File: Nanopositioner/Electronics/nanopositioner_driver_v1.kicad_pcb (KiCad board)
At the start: 2 copper layers, 9 parts, among them IC1 DLPC1438ZEZ, U1 ISO7720D, U2 DAC8552, U3 DAC8552, U4 STM32G431CBTx, U5 OPA552U, U6 ISO7720D, U7 OPA552U, U8 OPA552U

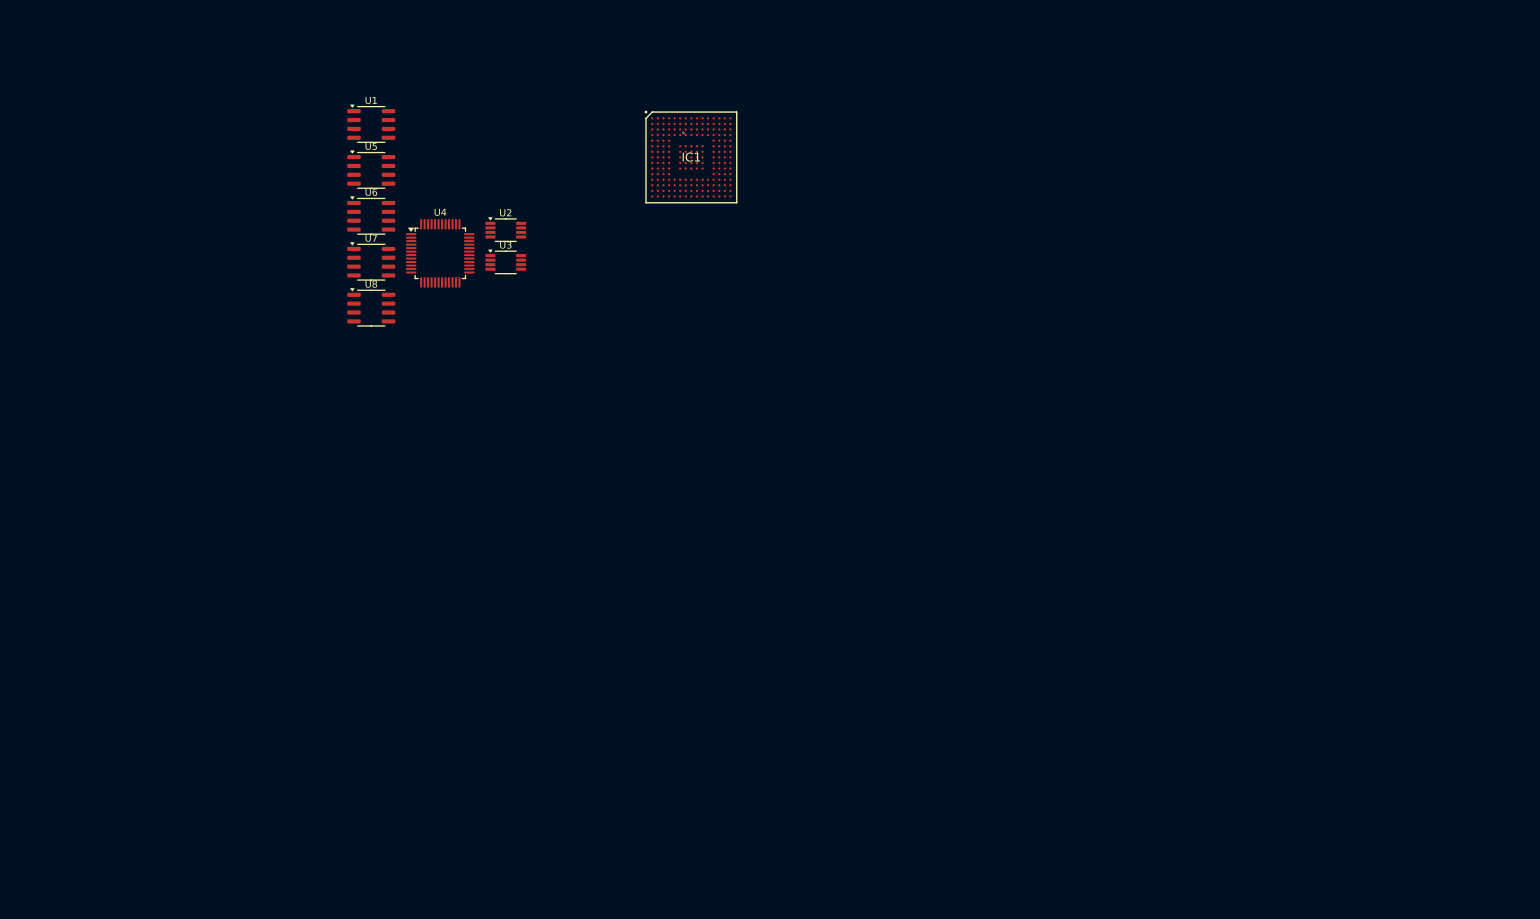
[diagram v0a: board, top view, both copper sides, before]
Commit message: Updated driver design
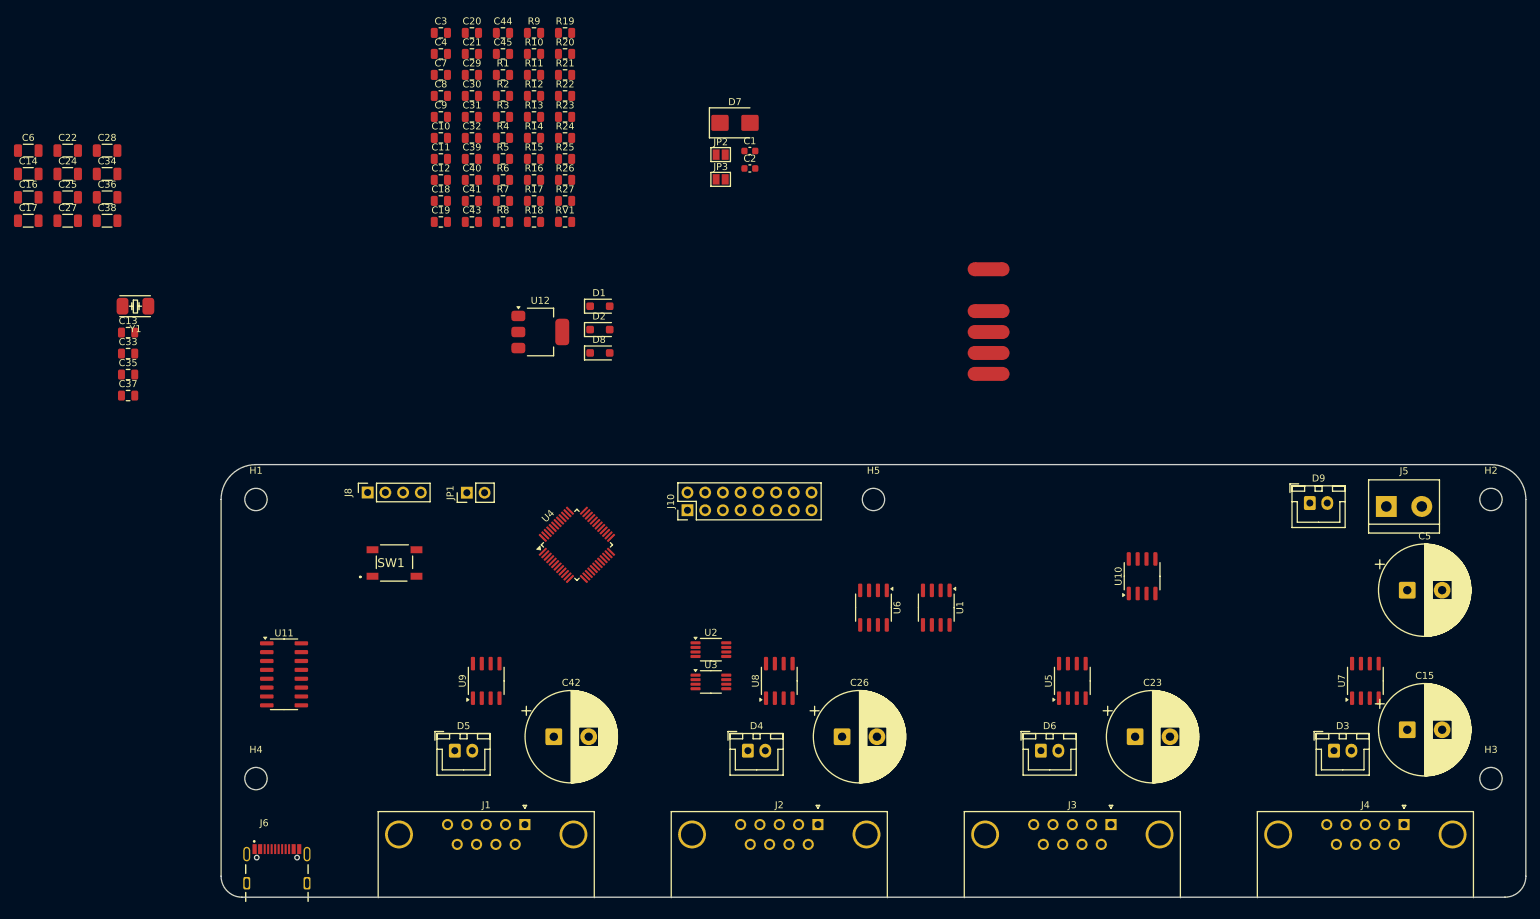
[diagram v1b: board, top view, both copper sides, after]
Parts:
- removed IC1: DLPC1438ZEZ, SamacSys_Parts:BGA201C80P15X15_1300X1300X100
- added C1: 22p, Capacitor_SMD:C_0603_1608Metric, F.Cu at (143.8, 38.0)
- added C10: 100n, Capacitor_SMD:C_0805_2012Metric, F.Cu at (99.5, 36.2)
- added C11: 100n, Capacitor_SMD:C_0805_2012Metric, F.Cu at (99.5, 39.2)
- added C12: 100n, Capacitor_SMD:C_0805_2012Metric, F.Cu at (99.5, 42.2)
- added C13: 100n 100V, Capacitor_SMD:C_0805_2012Metric, F.Cu at (54.7, 64.1)
- added C14: 1u 100V, Capacitor_SMD:C_1206_3216Metric, F.Cu at (40.4, 41.4)
- added C15: 220u 100V, Capacitor_THT:CP_Radial_D13.0mm_P5.00mm, F.Cu at (238.0, 121.0)
- added C16: 1u 100V, Capacitor_SMD:C_1206_3216Metric, F.Cu at (40.4, 44.7)
- added C17: 1u 100V, Capacitor_SMD:C_1206_3216Metric, F.Cu at (40.4, 48.0)
- added C18: 10u, Capacitor_SMD:C_0805_2012Metric, F.Cu at (99.5, 45.2)
- added C19: 10u, Capacitor_SMD:C_0805_2012Metric, F.Cu at (99.5, 48.2)
- added C2: 22p, Capacitor_SMD:C_0603_1608Metric, F.Cu at (143.8, 40.6)
- added C20: 10u, Capacitor_SMD:C_0805_2012Metric, F.Cu at (104.0, 21.1)
- added C21: 10u, Capacitor_SMD:C_0805_2012Metric, F.Cu at (104.0, 24.1)
- added C22: 1u 100V, Capacitor_SMD:C_1206_3216Metric, F.Cu at (46.0, 38.0)
- added C23: 220u 100V, Capacitor_THT:CP_Radial_D13.0mm_P5.00mm, F.Cu at (199.0, 122.0)
- added C24: 1u 100V, Capacitor_SMD:C_1206_3216Metric, F.Cu at (46.0, 41.4)
- added C25: 1u 100V, Capacitor_SMD:C_1206_3216Metric, F.Cu at (46.0, 44.7)
- added C26: 220u 100V, Capacitor_THT:CP_Radial_D13.0mm_P5.00mm, F.Cu at (157.0, 122.0)
- added C27: 1u 100V, Capacitor_SMD:C_1206_3216Metric, F.Cu at (46.0, 48.0)
- added C28: 1u 100V, Capacitor_SMD:C_1206_3216Metric, F.Cu at (51.7, 38.0)
- added C29: 10u, Capacitor_SMD:C_0805_2012Metric, F.Cu at (104.0, 27.1)
- added C3: 100n, Capacitor_SMD:C_0805_2012Metric, F.Cu at (99.5, 21.1)
- added C30: 100n, Capacitor_SMD:C_0805_2012Metric, F.Cu at (104.0, 30.2)
- added C31: 10u, Capacitor_SMD:C_0805_2012Metric, F.Cu at (104.0, 33.2)
- added C32: 100n, Capacitor_SMD:C_0805_2012Metric, F.Cu at (104.0, 36.2)
- added C33: 100n 100V, Capacitor_SMD:C_0805_2012Metric, F.Cu at (54.7, 67.1)
- added C34: 1u 100V, Capacitor_SMD:C_1206_3216Metric, F.Cu at (51.7, 41.4)
- added C35: 100n 100V, Capacitor_SMD:C_0805_2012Metric, F.Cu at (54.7, 70.1)
- added C36: 1u 100V, Capacitor_SMD:C_1206_3216Metric, F.Cu at (51.7, 44.7)
- added C37: 100n 100V, Capacitor_SMD:C_0805_2012Metric, F.Cu at (54.7, 73.1)
- added C38: 1u 100V, Capacitor_SMD:C_1206_3216Metric, F.Cu at (51.7, 48.0)
- added C39: 10u, Capacitor_SMD:C_0805_2012Metric, F.Cu at (104.0, 39.2)
- added C4: 10u, Capacitor_SMD:C_0805_2012Metric, F.Cu at (99.5, 24.1)
- added C40: 100n, Capacitor_SMD:C_0805_2012Metric, F.Cu at (104.0, 42.2)
- added C41: 100n, Capacitor_SMD:C_0805_2012Metric, F.Cu at (104.0, 45.2)
- added C42: 220u 100V, Capacitor_THT:CP_Radial_D13.0mm_P5.00mm, F.Cu at (115.7, 122.0)
- added C43: 100n, Capacitor_SMD:C_0805_2012Metric, F.Cu at (104.0, 48.2)
- added C44: 10u, Capacitor_SMD:C_0805_2012Metric, F.Cu at (108.4, 21.1)
- added C45: 10u, Capacitor_SMD:C_0805_2012Metric, F.Cu at (108.4, 24.1)
- added C5: 220u 100V, Capacitor_THT:CP_Radial_D13.0mm_P5.00mm, F.Cu at (238.0, 101.0)
- added C6: 1u 100V, Capacitor_SMD:C_1206_3216Metric, F.Cu at (40.4, 38.0)
- added C7: 100n, Capacitor_SMD:C_0805_2012Metric, F.Cu at (99.5, 27.1)
- added C8: 100n, Capacitor_SMD:C_0805_2012Metric, F.Cu at (99.5, 30.2)
- added C9: 100n, Capacitor_SMD:C_0805_2012Metric, F.Cu at (99.5, 33.2)
- added D1: BZT52-C5V6, Diode_SMD:D_SOD-123F, F.Cu at (122.3, 60.3)
- added D2: BZT52-C5V6, Diode_SMD:D_SOD-123F, F.Cu at (122.3, 63.6)
- added D3: LED_Small, Connector_JST:JST_XH_B2B-XH-A_1x02_P2.50mm_Vertical, F.Cu at (227.5, 124.0)
- added D4: LED_Small, Connector_JST:JST_XH_B2B-XH-A_1x02_P2.50mm_Vertical, F.Cu at (143.5, 124.0)
- added D5: LED_Small, Connector_JST:JST_XH_B2B-XH-A_1x02_P2.50mm_Vertical, F.Cu at (101.5, 124.0)
- added D6: LED_Small, Connector_JST:JST_XH_B2B-XH-A_1x02_P2.50mm_Vertical, F.Cu at (185.5, 124.0)
- added D7: SS310, Diode_SMD:D_SMB, F.Cu at (141.6, 34.0)
- added D8: BZT52-B75, Diode_SMD:D_SOD-123F, F.Cu at (122.3, 67.0)
- added D9: OVP_INDICATOR, Connector_JST:JST_XH_B2B-XH-A_1x02_P2.50mm_Vertical, F.Cu at (224.0, 88.5)
- added H1: MountingHole, MountingHole:MountingHole_3.2mm_M3, F.Cu at (73.0, 88.0)
- added H2: MountingHole, MountingHole:MountingHole_3.2mm_M3, F.Cu at (250.0, 88.0)
- added H3: MountingHole, MountingHole:MountingHole_3.2mm_M3, F.Cu at (250.0, 128.0)
- added H4: MountingHole, MountingHole:MountingHole_3.2mm_M3, F.Cu at (73.0, 128.0)
- added H5: MountingHole, MountingHole:MountingHole_3.2mm_M3, F.Cu at (161.5, 88.0)
- added J1: DE9_Pins, Connector_Dsub:DSUB-9_Socket_Horizontal_P2.77x2.84mm_EdgePinOffset7.70mm_Housed_MountingHolesOffset9.12mm, F.Cu at (111.5, 134.6)
- added J10: Conn_02x08_Odd_Even, Connector_PinHeader_2.54mm:PinHeader_2x08_P2.54mm_Vertical, F.Cu at (134.8, 89.5)
- added J2: DE9_Pins, Connector_Dsub:DSUB-9_Socket_Horizontal_P2.77x2.84mm_EdgePinOffset7.70mm_Housed_MountingHolesOffset9.12mm, F.Cu at (153.5, 134.6)
- added J3: DE9_Pins, Connector_Dsub:DSUB-9_Socket_Horizontal_P2.77x2.84mm_EdgePinOffset7.70mm_Housed_MountingHolesOffset9.12mm, F.Cu at (195.5, 134.6)
- added J4: DE9_Pins, Connector_Dsub:DSUB-9_Socket_Horizontal_P2.77x2.84mm_EdgePinOffset7.70mm_Housed_MountingHolesOffset9.12mm, F.Cu at (237.5, 134.6)
- added J5: HV_IN, TerminalBlock:TerminalBlock_bornier-2_P5.08mm, F.Cu at (235.0, 89.0)
- added J6: USB_UART_RECEPTACLE, SamacSys_Parts:GCT_USB4105GFA120, F.Cu at (76.0, 143.0)
- added J8: SWD, Connector_PinSocket_2.54mm:PinSocket_1x04_P2.54mm_Vertical, F.Cu at (89.0, 87.0)
- added JP1: BOOT0, Connector_PinHeader_2.54mm:PinHeader_1x02_P2.54mm_Vertical, F.Cu at (103.2, 87.0)
- added JP2: 5V_TEST, Jumper:SolderJumper-2_P1.3mm_Open_Pad1.0x1.5mm, F.Cu at (139.6, 38.6)
- added JP3: 6V2_TEST, Jumper:SolderJumper-2_P1.3mm_Open_Pad1.0x1.5mm, F.Cu at (139.6, 42.1)
- added NT2: VDDA, NetTie:NetTie-2_SMD_Pad2.0mm, F.Cu at (178.0, 55.0)
- added NT4: NetTie_2, NetTie:NetTie-2_SMD_Pad2.0mm, F.Cu at (178.0, 61.0)
- added NT5: NetTie_2, NetTie:NetTie-2_SMD_Pad2.0mm, F.Cu at (178.0, 64.0)
- added NT6: NetTie_2, NetTie:NetTie-2_SMD_Pad2.0mm, F.Cu at (178.0, 67.0)
- added NT7: NetTie_2, NetTie:NetTie-2_SMD_Pad2.0mm, F.Cu at (178.0, 70.0)
- added R1: 20k, Capacitor_SMD:C_0805_2012Metric, F.Cu at (108.4, 27.1)
- added R10: 180k, Capacitor_SMD:C_0805_2012Metric, F.Cu at (112.8, 24.1)
- added R11: 200, Capacitor_SMD:C_0805_2012Metric, F.Cu at (112.8, 27.1)
- added R12: 20k, Capacitor_SMD:C_0805_2012Metric, F.Cu at (112.8, 30.2)
- added R13: 200, Capacitor_SMD:C_0805_2012Metric, F.Cu at (112.8, 33.2)
- added R14: 200, Capacitor_SMD:C_0805_2012Metric, F.Cu at (112.8, 36.2)
- added R15: 200, Capacitor_SMD:C_0805_2012Metric, F.Cu at (112.8, 39.2)
- added R16: 180k, Capacitor_SMD:C_0805_2012Metric, F.Cu at (112.8, 42.2)
- added R17: 20k, Capacitor_SMD:C_0805_2012Metric, F.Cu at (112.8, 45.2)
- added R18: 20k, Capacitor_SMD:C_0805_2012Metric, F.Cu at (112.8, 48.2)
- added R19: 1k, Capacitor_SMD:C_0805_2012Metric, F.Cu at (117.3, 21.1)
- added R2: 180k, Capacitor_SMD:C_0805_2012Metric, F.Cu at (108.4, 30.2)
- added R20: 1k, Capacitor_SMD:C_0805_2012Metric, F.Cu at (117.3, 24.1)
- added R21: 1k, Capacitor_SMD:C_0805_2012Metric, F.Cu at (117.3, 27.1)
- added R22: 1k, Capacitor_SMD:C_0805_2012Metric, F.Cu at (117.3, 30.2)
- added R23: 10M, Capacitor_SMD:C_0805_2012Metric, F.Cu at (117.3, 33.2)
- added R24: 100k, Capacitor_SMD:C_0805_2012Metric, F.Cu at (117.3, 36.2)
- added R25: 5k49, Capacitor_SMD:C_0805_2012Metric, F.Cu at (117.3, 39.2)
- added R26: 5k49, Capacitor_SMD:C_0805_2012Metric, F.Cu at (117.3, 42.2)
- added R27: 100k, Capacitor_SMD:C_0805_2012Metric, F.Cu at (117.3, 45.2)
- added R3: 10k, Capacitor_SMD:C_0805_2012Metric, F.Cu at (108.4, 33.2)
- added R4: 0, Capacitor_SMD:C_0805_2012Metric, F.Cu at (108.4, 36.2)
- added R5: 0, Capacitor_SMD:C_0805_2012Metric, F.Cu at (108.4, 39.2)
- added R6: 180k, Capacitor_SMD:C_0805_2012Metric, F.Cu at (108.4, 42.2)
- added R7: 20k, Capacitor_SMD:C_0805_2012Metric, F.Cu at (108.4, 45.2)
- added R8: 10k, Capacitor_SMD:C_0805_2012Metric, F.Cu at (108.4, 48.2)
- added R9: 20k, Capacitor_SMD:C_0805_2012Metric, F.Cu at (112.8, 21.1)
- added RV1: 1M, Capacitor_SMD:C_0805_2012Metric, F.Cu at (117.3, 48.2)
- added SW1: NRST, SamacSys_Parts:TL3342F260QG, F.Cu at (92.8, 97.1)
- added U10: REF5050AD, Package_SO:SOIC-8_3.9x4.9mm_P1.27mm, F.Cu at (200.0, 99.0)
- added U11: CH340C, Package_SO:SOIC-16_3.9x9.9mm_P1.27mm, F.Cu at (77.0, 113.1)
- added U12: AMS1117-3.3, Package_TO_SOT_SMD:SOT-223-3_TabPin2, F.Cu at (113.8, 64.0)
- added U9: OPA552U, Package_SO:SOIC-8_3.9x4.9mm_P1.27mm, F.Cu at (106.0, 114.0)
- added Y1: 8MHz, SamacSys_Parts:YSX530, F.Cu at (55.7, 60.3)
- moved U7 154.6 mm to (232.0, 114.0), turned to 90 degrees
- moved U5 124.3 mm to (190.0, 114.0), turned to 90 degrees
- moved U1 106.5 mm to (170.5, 103.5), turned to -90 degrees
- moved U6 91.3 mm to (161.5, 103.5), turned to -90 degrees
- moved U8 79.2 mm to (148.0, 114.0), turned to 90 degrees
- moved U2 66.9 mm to (138.2, 109.5)
- moved U3 66.9 mm to (138.2, 114.2)
- moved U4 46.1 mm to (119.0, 94.5), turned to 45 degrees
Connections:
- net Net-(U1-OUTA) renamed /~{SYNC1}
- net Net-(U1-OUTB) renamed /~{SYNC2}
- net Net-(U2-D_{IN}) renamed /DIN
- net Net-(U2-SCLK) renamed /SCLK
- U1 pad 1: unconnected-(U1-VCC1-Pad1) -> +3V3
- U2 pad 1: unconnected-(U2-V_{DD}-Pad1) -> +5V_HV
- U2 pad 2: unconnected-(U2-V_{REF}-Pad2) -> +5V_REF
- U3 pad 1: unconnected-(U3-V_{DD}-Pad1) -> +5V_HV
- U3 pad 2: unconnected-(U3-V_{REF}-Pad2) -> +5V_REF
- U3 pad 3: unconnected-(U3-V_{OUT}B-Pad3) -> /PIEZO_CH4_SIG
- U4 pad 1: /VDD -> +3V3
- U4 pad 10: unconnected-(U4-PA2-Pad10) -> /UART2_TX
- U4 pad 11: unconnected-(U4-PA3-Pad11) -> /UART2_RX
- U4 pad 16: unconnected-(U4-PB0-Pad16) -> /PB0
- U4 pad 17: unconnected-(U4-PB1-Pad17) -> /~{CS4}
- U4 pad 18: unconnected-(U4-PB2-Pad18) -> /~{CS3}
- U4 pad 2: unconnected-(U4-PC13-Pad2) -> /PC13
- U4 pad 21: /VDDA -> +3V3
- U4 pad 22: unconnected-(U4-PB10-Pad22) -> /BTN3
- U4 pad 24: /VDD -> +3V3
- U4 pad 25: unconnected-(U4-PB11-Pad25) -> /~{CS2}
- U4 pad 26: unconnected-(U4-PB12-Pad26) -> /~{CS1}
- U4 pad 27: unconnected-(U4-PB13-Pad27) -> /CLK1_2
- U4 pad 28: unconnected-(U4-PB14-Pad28) -> /DO1
- U4 pad 29: unconnected-(U4-PB15-Pad29) -> /DIN1
- U4 pad 3: unconnected-(U4-PC14-Pad3) -> /PC14
- U4 pad 30: unconnected-(U4-PA8-Pad30) -> /CONN_TEST_1_P
- U4 pad 31: unconnected-(U4-PA9-Pad31) -> /CONN_TEST_2_P
- U4 pad 32: unconnected-(U4-PA10-Pad32) -> /CONN_TEST_3_P
- U4 pad 33: unconnected-(U4-PA11-Pad33) -> /CONN_TEST_4_P
- U4 pad 34: unconnected-(U4-PA12-Pad34) -> /BTN1
- U4 pad 36: /VDD -> +3V3
- U4 pad 37: unconnected-(U4-PA13-Pad37) -> /SWDIO
- U4 pad 38: unconnected-(U4-PA14-Pad38) -> /SWCLK
- U4 pad 39: unconnected-(U4-PA15-Pad39) -> /BTN4
- U4 pad 4: unconnected-(U4-PC15-Pad4) -> /PC15
- U4 pad 40: unconnected-(U4-PB3-Pad40) -> /CLK3_4
- U4 pad 41: unconnected-(U4-PB4-Pad41) -> /DO3
- U4 pad 42: unconnected-(U4-PB5-Pad42) -> /DIN3
- U4 pad 43: unconnected-(U4-PB6-Pad43) -> /UART1_TX
- U4 pad 44: unconnected-(U4-PB7-Pad44) -> /UART1_RX
- U4 pad 46: unconnected-(U4-PB9-Pad46) -> /BTN2
- U4 pad 48: /VDD -> +3V3
- U4 pad 8: unconnected-(U4-PA0-Pad8) -> /BTN5
- U4 pad 9: unconnected-(U4-PA1-Pad9) -> /BTN6
- U5 pad 2: unconnected-(U5---Pad2) -> Net-(U5--)
- U5 pad 6: unconnected-(U5-Pad6) -> Net-(Q3-B)
- U6 pad 1: unconnected-(U6-VCC1-Pad1) -> +3V3
- U7 pad 2: unconnected-(U7---Pad2) -> Net-(U7--)
- U7 pad 3: /PIEZO_CH2_SIG -> /PIEZO_CH4_SIG
- U7 pad 6: unconnected-(U7-Pad6) -> Net-(Q5-B)
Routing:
- net unconnected-(IC1-VDD_4-PadD7): track 0.51 -> 0.00 mm, vias 1 -> 0
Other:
- board outline added: 187 x 62 mm
- board text added: "High Voltage"
- board text added: "Low Voltage"

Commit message: Updated the complete PCB design
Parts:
- removed NT2: VDDA, NetTie:NetTie-2_SMD_Pad2.0mm
- removed NT4, NT5, NT6, NT7: NetTie_2, NetTie:NetTie-2_SMD_Pad2.0mm
- removed R17, R18: 20k, Capacitor_SMD:C_0805_2012Metric
- added C46: 100n, Capacitor_SMD:C_0805_2012Metric, F.Cu at (163.7, 99.6)
- added C47: 100n, Capacitor_SMD:C_0805_2012Metric, F.Cu at (172.7, 99.6)
- added C48: 100n, Capacitor_SMD:C_0805_2012Metric, F.Cu at (165.5, 109.2)
- added C49: 100n, Capacitor_SMD:C_0805_2012Metric, F.Cu at (174.5, 109.2)
- added C50: 220p 100V, Capacitor_SMD:C_1206_3216Metric, F.Cu at (237.6, 115.1)
- added C51: C_CAP, Capacitor_SMD:C_0805_2012Metric, F.Cu at (243.0, 115.4)
- added C52: C_CAP, Capacitor_SMD:C_0805_2012Metric, F.Cu at (200.3, 114.7)
- added C53: 220p 100V, Capacitor_SMD:C_1206_3216Metric, F.Cu at (196.1, 114.8)
- added C54: C_CAP, Capacitor_SMD:C_0805_2012Metric, F.Cu at (158.5, 114.8)
- added C55: 220p 100V, Capacitor_SMD:C_1206_3216Metric, F.Cu at (154.1, 114.8)
- added C56: C_CAP, Capacitor_SMD:C_0805_2012Metric, F.Cu at (116.5, 114.8)
- added C57: 220p 100V, Capacitor_SMD:C_1206_3216Metric, F.Cu at (112.1, 114.8)
- added D10: PIEZO_SUPPLY_IND, Connector_JST:JST_XH_B2B-XH-A_1x02_P2.50mm_Vertical, F.Cu at (215.1, 87.6)
- added D11: 5V_SUPPLY, Connector_JST:JST_XH_B2B-XH-A_1x02_P2.50mm_Vertical, F.Cu at (134.2, 87.6)
- added H6: MountingHole, MountingHole:MountingHole_3.2mm_M3, F.Cu at (169.0, 137.0)
- added Q1: MJD45H11T4G, SamacSys_Parts:MJD45H11AJ, F.Cu at (136.5, 124.0)
- added Q10: BCX56, Package_TO_SOT_SMD:SOT-89-3, F.Cu at (193.0, 87.5)
- added Q11: NCE1540K, Package_TO_SOT_SMD:TO-252-2, F.Cu at (232.3, 100.8)
- added Q12: NCE1540K, Package_TO_SOT_SMD:TO-252-2, F.Cu at (239.6, 100.8)
- added Q2: MJD44H11T4G, SamacSys_Parts:MJD44H11AJ, F.Cu at (145.5, 124.0)
- added Q3: MJD45H11T4G, SamacSys_Parts:MJD45H11AJ, F.Cu at (94.5, 124.0)
- added Q4: MJD44H11T4G, SamacSys_Parts:MJD44H11AJ, F.Cu at (103.5, 124.0)
- added Q5: MJD45H11T4G, SamacSys_Parts:MJD45H11AJ, F.Cu at (178.6, 124.0)
- added Q6: MJD44H11T4G, SamacSys_Parts:MJD44H11AJ, F.Cu at (187.5, 124.0)
- added Q7: MJD45H11T4G, SamacSys_Parts:MJD45H11AJ, F.Cu at (220.5, 124.0)
- added Q8: MJD44H11T4G, SamacSys_Parts:MJD44H11AJ, F.Cu at (229.5, 124.0)
- added Q9: BCX56, Package_TO_SOT_SMD:SOT-89-3, F.Cu at (193.1, 99.5)
- added R28: 0, Resistor_SMD:R_0805_2012Metric, F.Cu at (170.5, 99.6)
- added R29: 0, Resistor_SMD:R_0805_2012Metric, F.Cu at (168.5, 99.6)
- added R30: 5, Resistor_SMD:R_0805_2012Metric, F.Cu at (142.8, 132.0)
- added R31: 5, Resistor_SMD:R_0805_2012Metric, F.Cu at (100.9, 132.0)
- added R32: 5, Resistor_SMD:R_0805_2012Metric, F.Cu at (184.9, 132.0)
- added R33: 5, Resistor_SMD:R_0805_2012Metric, F.Cu at (226.8, 132.0)
- added R34: 10k, Resistor_SMD:R_0805_2012Metric, F.Cu at (213.8, 93.2)
- added R35: 10k, Resistor_SMD:R_0805_2012Metric, F.Cu at (139.0, 87.4)
- added RV2: 100k, Potentiometer_THT:Potentiometer_Bourns_3266W_Vertical, F.Cu at (211.6, 113.2)
- added RV3: 100k, Potentiometer_THT:Potentiometer_Bourns_3266W_Vertical, F.Cu at (208.2, 101.5)
- added TP1: CH2_OUTPUT, TestPoint:TestPoint_Pad_D1.0mm, F.Cu at (169.1, 124.8)
- added TP10: CH3_OPA_OUT, TestPoint:TestPoint_Pad_D1.0mm, F.Cu at (172.1, 124.1)
- added TP11: CH2_OPA_OUT, TestPoint:TestPoint_Pad_D1.0mm, F.Cu at (129.3, 127.5)
- added TP12: CH1_OPA_OUT, TestPoint:TestPoint_Pad_D1.0mm, F.Cu at (97.2, 107.5)
- added TP13: 60V_TEST, TestPoint:TestPoint_Pad_D1.0mm, F.Cu at (219.3, 92.7)
- added TP14: 5V_TEST, TestPoint:TestPoint_Pad_D1.0mm, F.Cu at (209.6, 106.7)
- added TP15: 6V2_TEST, TestPoint:TestPoint_Pad_D1.0mm, F.Cu at (189.6, 96.5)
- added TP16: GNDV_TESTPOINT, TestPoint:TestPoint_Pad_D1.0mm, F.Cu at (213.9, 96.4)
- added TP17: GNDV_TESTPOINT, TestPoint:TestPoint_Pad_D1.0mm, F.Cu at (189.6, 103.8)
- added TP18: GNDV_TESTPOINT, TestPoint:TestPoint_Pad_D1.0mm, F.Cu at (209.3, 120.2)
- added TP19: GNDV_TESTPOINT, TestPoint:TestPoint_Pad_D1.0mm, F.Cu at (127.3, 135.0)
- added TP2: CH1_OUTPUT, TestPoint:TestPoint_Pad_D1.0mm, F.Cu at (125.0, 127.5)
- added TP20: 5V_VREF_TEST, TestPoint:TestPoint_Pad_D1.0mm, F.Cu at (162.7, 114.3)
- added TP21: GNDV_TESTPOINT, TestPoint:TestPoint_Pad_D1.0mm, F.Cu at (250.3, 139.4)
- added TP22: GNDV_TESTPOINT, TestPoint:TestPoint_Pad_D1.0mm, F.Cu at (169.1, 117.3)
- added TP23: GNDV_TESTPOINT, TestPoint:TestPoint_Pad_D1.0mm, F.Cu at (126.2, 121.8)
- added TP24: GNDV_TESTPOINT, TestPoint:TestPoint_Pad_D1.0mm, F.Cu at (91.0, 110.9)
- added TP25: GNDV_TESTPOINT, TestPoint:TestPoint_Pad_D1.0mm, F.Cu at (210.9, 135.1)
- added TP26: SCLK_TP, TestPoint:TestPoint_Pad_D1.0mm, F.Cu at (164.0, 112.4)
- added TP27: DIN_TP, TestPoint:TestPoint_Pad_D1.0mm, F.Cu at (168.0, 110.9)
- added TP28: L_SCLK_TP, TestPoint:TestPoint_Pad_D1.0mm, F.Cu at (151.5, 102.1)
- added TP29: L_DIN_TP, TestPoint:TestPoint_Pad_D1.0mm, F.Cu at (155.4, 102.1)
- added TP3: CH3_OUTPUT, TestPoint:TestPoint_Pad_D1.0mm, F.Cu at (210.9, 127.4)
- added TP30: XTAL_0_TP, TestPoint:TestPoint_Pad_D1.0mm, F.Cu at (131.0, 98.6)
- added TP31: XTAL_1_TP, TestPoint:TestPoint_Pad_D1.0mm, F.Cu at (130.9, 94.0)
- added TP32: GND_TP, TestPoint:TestPoint_Pad_D1.0mm, F.Cu at (151.5, 95.4)
- added TP33: GND_TP, TestPoint:TestPoint_Pad_D1.0mm, F.Cu at (155.4, 95.4)
- added TP4: CH4_OUTPUT, TestPoint:TestPoint_Pad_D1.0mm, F.Cu at (250.3, 132.0)
- added TP5: CH4_AN_IN, TestPoint:TestPoint_Pad_D1.0mm, F.Cu at (207.2, 113.8)
- added TP6: CH3_AN_IN, TestPoint:TestPoint_Pad_D1.0mm, F.Cu at (204.1, 116.1)
- added TP7: CH2_AN_IN, TestPoint:TestPoint_Pad_D1.0mm, F.Cu at (129.0, 115.4)
- added TP8: CH1_AN_IN, TestPoint:TestPoint_Pad_D1.0mm, F.Cu at (123.3, 115.4)
- added TP9: CH4_OPA_OUT, TestPoint:TestPoint_Pad_D1.0mm, F.Cu at (214.0, 128.0)
- D1, D2: value BZT52-C5V6 -> BZT52-C6V2
- R1, R10, R11, R12, R13, R14, R15, R16, R19, R2, R20, R21, R22, R23, R24, R25, R26, R27, R3, R4, R5, R6, R7, R8, R9: footprint Capacitor_SMD:C_0805_2012Metric -> Resistor_SMD:R_0805_2012Metric
- RV1: footprint Capacitor_SMD:C_0805_2012Metric -> Potentiometer_THT:Potentiometer_Bourns_3266W_Vertical
- moved C17 201.9 mm to (230.8, 115.0), turned to 90 degrees
- moved C16 200.8 mm to (228.5, 115.0), turned to 90 degrees
- moved C34 186.6 mm to (224.0, 113.0), turned to 180 degrees
- moved C33 175.3 mm to (224.6, 110.5), turned to 180 degrees
- moved C25 159.3 mm to (189.0, 115.0), turned to 90 degrees
- moved C24 158.6 mm to (186.5, 115.0), turned to 90 degrees
- moved D3 154.5 mm to (73.0, 120.8), turned to -90 degrees
- moved R12 147.9 mm to (237.0, 110.5)
- moved R23 146.9 mm to (243.0, 109.2), turned to 180 degrees
- moved R24 146.4 mm to (243.0, 111.3), turned to 180 degrees
- moved C38 145.6 mm to (182.0, 113.0), turned to 180 degrees
- moved R15 144.1 mm to (223.1, 132.0), turned to 180 degrees
- moved R27 143.0 mm to (243.0, 113.4)
- moved RV1 142.9 mm to (250.5, 99.9)
- moved R16 142.7 mm to (237.0, 112.5)
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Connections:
- C30 pad 1: GND -> GNDV
- C31 pad 1: GND -> GNDV
- C32 pad 1: GND -> GNDV
- C39 pad 1: GND -> GNDV
- C7 pad 2: /VREF+ -> +3V3
- J1 pad 2: /DIN2 -> /DIN1
- J1 pad 7: /DO2 -> /DO1
- J10 pad 1: /BTN1 -> unconnected-(J10-Pin_1-Pad1)
- J10 pad 10: +3V3 -> +5V
- J10 pad 12: +5V -> +3V3
- J10 pad 2: /PC13 -> /BTN1
- J10 pad 3: /BTN2 -> unconnected-(J10-Pin_3-Pad3)
- J10 pad 4: /PC14 -> /BTN2
- J10 pad 5: /BTN3 -> unconnected-(J10-Pin_5-Pad5)
- J10 pad 6: /PC15 -> /BTN3
- J10 pad 7: /BTN4 -> unconnected-(J10-Pin_7-Pad7)
- J10 pad 8: /PB0 -> /BTN4
- J4 pad 2: /DIN4 -> /DIN3
- J4 pad 7: /DO4 -> /DO3
- J6 pad SH1: (no net) -> GND
- J6 pad SH2: (no net) -> GND
- J6 pad SH3: (no net) -> GND
- J6 pad SH4: (no net) -> GND
- R10 pad 1: /PIEZO_CH1_PA -> Net-(Q3-E)
- R11 pad 1: /PIEZO_CH1_PA -> Net-(Q3-E)
- R13 pad 1: /PIEZO_CH2_PA -> Net-(Q1-E)
- R14 pad 1: /PIEZO_CH3_PA -> Net-(Q5-E)
- R15 pad 1: /PIEZO_CH4_PA -> Net-(Q7-E)
- R16 pad 1: /PIEZO_CH4_PA -> Net-(Q7-E)
- R2 pad 1: /PIEZO_CH2_PA -> Net-(Q1-E)
- R6 pad 1: /PIEZO_CH3_PA -> Net-(Q5-E)
- U4 pad 12: Net-(U1-INA) -> /BTN4
- U4 pad 14: Net-(U1-INB) -> Net-(U4-PA6)
- U4 pad 16: /PB0 -> Net-(U4-PB0)
- U4 pad 17: /~{CS4} -> unconnected-(U4-PB1-Pad17)
- U4 pad 18: /~{CS3} -> /~{CS1}
- U4 pad 2: /PC13 -> /BTN1
- U4 pad 20: /VREF+ -> +3V3
- U4 pad 22: /BTN3 -> unconnected-(U4-PB10-Pad22)
- U4 pad 25: /~{CS2} -> unconnected-(U4-PB11-Pad25)
- U4 pad 26: /~{CS1} -> /~{CS4}
- U4 pad 3: /PC14 -> /BTN2
- U4 pad 30: /CONN_TEST_1_P -> /CONN_TEST_4_P
- U4 pad 31: /CONN_TEST_2_P -> /CONN_TEST_3_P
- U4 pad 32: /CONN_TEST_3_P -> /CONN_TEST_2_P
- U4 pad 33: /CONN_TEST_4_P -> /CONN_TEST_1_P
- U4 pad 34: /BTN1 -> unconnected-(U4-PA12-Pad34)
- U4 pad 39: /BTN4 -> /~{CS3}
- U4 pad 4: /PC15 -> /BTN3
- U4 pad 46: /BTN2 -> /~{CS2}
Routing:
- net +5V: track 0.00 -> 592.2 mm, vias 0 -> 11
- net GND: track 0.00 -> 304.6 mm, vias 0 -> 28
- net +3V3: track 0.00 -> 286.1 mm, vias 0 -> 12
- net /~{CS4}: track 0.00 -> 261.9 mm, vias 0 -> 2
- net /CLK3_4: track 0.00 -> 243.7 mm, vias 0 -> 2
- net /CONN_TEST_4_P: track 0.00 -> 222.0 mm, vias 0 -> 2
- net /~{CS3}: track 0.00 -> 219.9 mm, vias 0 -> 12
- net /DO3: track 0.00 -> 217.7 mm, vias 0 -> 1
- net /DIN3: track 0.00 -> 208.9 mm, vias 0 -> 2
- net /CONN_TEST_3_P: track 0.00 -> 177.8 mm, vias 0 -> 2
- net /CLK1_2: track 0.00 -> 154.9 mm, vias 0 -> 2
- net +60V: track 0.00 -> 153.0 mm, vias 0 -> 50
- net /DO1: track 0.00 -> 148.8 mm, vias 0 -> 2
- net /DIN1: track 0.00 -> 141.7 mm, vias 0 -> 4
- net /CONN_TEST_2_P: track 0.00 -> 134.5 mm, vias 0 -> 2
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- added copper zone on B.Cu, net +60V
- added copper zone on F.Cu, net +60V
- added copper zone on B.Cu, net GND
- added copper zone on F.Cu, net GND
- added copper zone on B.Cu, net GNDV
- added copper zone on F.Cu, net GNDV
- added copper zone on F.Cu, net Net-(Q1-E)
- added copper zone on F.Cu, net Net-(Q3-E)
- added copper zone on F.Cu, net Net-(Q5-E)
- added copper zone on F.Cu, net Net-(Q7-E)
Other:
- board text added: "JLCJLCJLCJLC"
- board text added: "RESET"
